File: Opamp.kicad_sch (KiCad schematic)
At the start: 51 parts, among them Q2 NPN, Q3 NPN, U1 ADA4522-2ARMZ-R7, U10 2N7002KDW_R1_00001, U11 2N7002KDW_R1_00001, U2 TCA9535RTWR, U4 2N7002KDW_R1_00001, U5 2N7002KDW_R1_00001, U6 2N7002KDW_R1_00001, U7 2N7002KDW_R1_00001, U8 2N7002KDW_R1_00001, U9 2N7002KDW_R1_00001

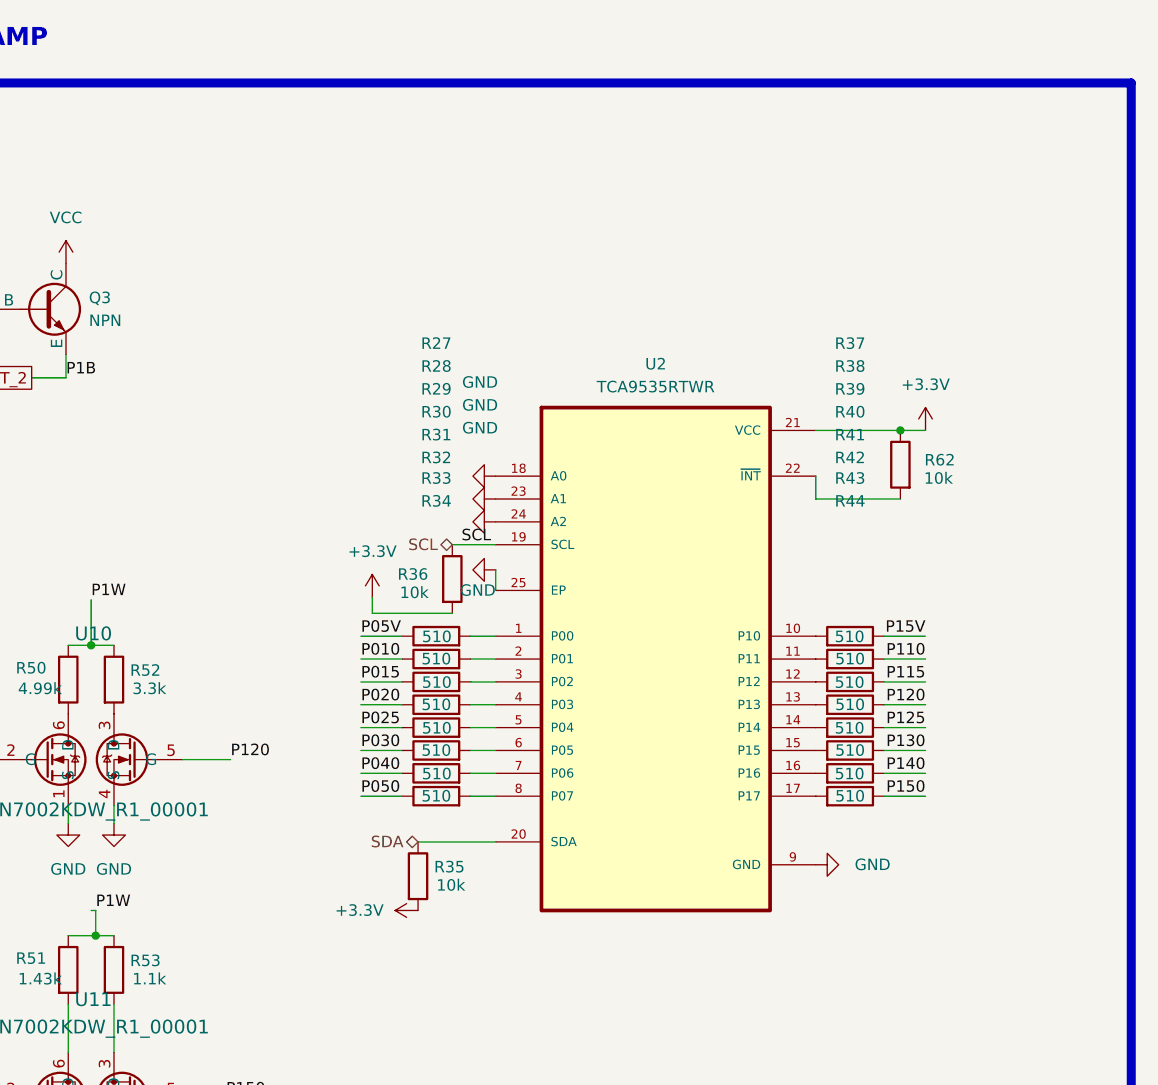
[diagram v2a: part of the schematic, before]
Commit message: version 4: changed GPIO expander, added current sense resistor to electrodes, added buzzer pins, fixed some gpio inputs that needs to be pulled high, added battery charge detection, added battery level measurement feature
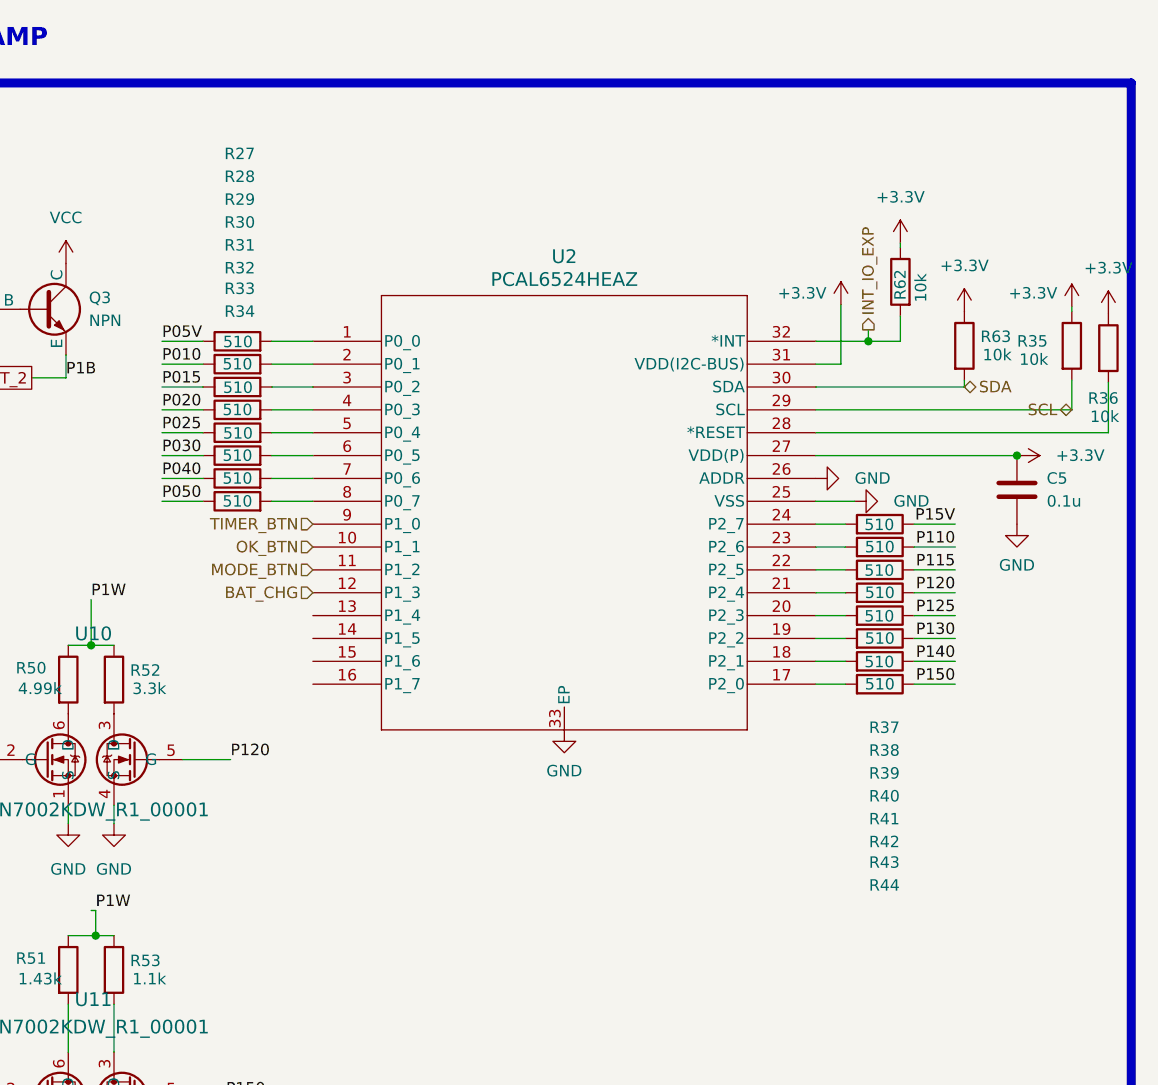
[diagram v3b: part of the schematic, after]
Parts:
- removed U2: TCA9535RTWR, Library:QFN50P400X400X80-25N, symbol 2023-09-03_14-36-57:TCA9535RTWR
- added C5: 0.1u, Capacitor_SMD:C_0402_1005Metric, symbol Device:C
- added R63: 10k, Resistor_SMD:R_0402_1005Metric, symbol Device:R
- added U2: PCAL6524HEAZ, Library:HUQFN32_PCAL6524_NXP, symbol 2023-09-03_14-36-57:PCAL6524HEAZ
- U1: Long Description (none) -> Zero-Drift Amplifier 2 Circuit Rail-to-Rail 8-MSOP
- U10, U11, U4, U5, U6, U7, U8, U9: Long Description (none) -> Mosfet Array 60V 115mA (Ta) 200mW (Ta) Surface Mount SOT-363
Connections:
- net +3.3V: now also R35.1, R36.1, C5.2, R63.1, U2.27 (VDD(P)), U2.31 (VDD(I2C-BUS)); no longer R35.2, R36.2
- net GND: now also C5.1, U2.25 (VSS), U2.26 (ADDR), U2.33 (EP)
- net SCL: now also R35.2, U2.29 (SCL); no longer R36.1
- net SDA: now also R63.2, U2.30 (SDA); no longer R35.1
- net at R41.2: now also U2.20 (P2_3)
- net at R31.2: now also U2.5 (P0_4)
- net at R30.2: now also U2.4 (P0_3)
- net at R44.2: now also U2.17 (P2_0)
- net at R37.2: now also U2.24 (P2_7)
- net INT_IO_EXP: now reaches R62.2
- net INT_IO_EXP: now also U2.32 (*INT)
- net at R27.2: now also U2.1 (P0_0)
- net at R38.2: now also U2.23 (P2_6)
- net at R39.2: now also U2.22 (P2_5)
- net at R40.2: now also U2.21 (P2_4)
- net at R42.2: now also U2.19 (P2_2)
- net at R43.2: now also U2.18 (P2_1)
- net at R28.2: now also U2.2 (P0_1)
- net at R29.2: now also U2.3 (P0_2)
- net at R32.2: now also U2.6 (P0_5)
- net at R33.2: now also U2.7 (P0_6)
- net at R34.2: now also U2.8 (P0_7)
- new net: R36.2, U2.28 (*RESET)
- new net BAT_CHG: U2.12 (P1_3)
- new net MODE_BTN: U2.11 (P1_2)
- new net OK_BTN: U2.10 (P1_1)
- new net TIMER_BTN: U2.9 (P1_0)
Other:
- moved on the sheet: R27, R28, R29, R30, R31, R32, R33, R34, R37, R38, R39, R40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

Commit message: version 5: replaced ESP32-WROVER module with ESP-Mini, removed 2.5mm plugs, changed USB connector and routed electrode signals on it, added RC snubber circuit to boost converter and output caps to reduce switching loop
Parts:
- Q2, Q3: Long Description Bipolar (BJT) Transistor NPN 60 V 2 A 100MHz 460 mW Surface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 -> Bipolar (BJT) Transistor NPN 60 V 1 A 150MHz 460 mW Surface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; Manufacturer On Semiconductor -> Diodes Incorporated; Manufacturer Part Number NSS60201LT1G -> DNBT8105-7
- R11, R45: Manufacturer Part Number RC0402FR-1016KL -> RC0402FR-0716KL
- R27, R28, R29, R30, R31, R32, R33, R34, R37, R38, R39, R40, R41, R42, R43, R44: Manufacturer Part Number RC0402FR-10510RL -> RC0402FR-07510RL
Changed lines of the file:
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@@
       (effects (font (size 1.27 1.27)) hide)
     )
-    (property "Manufacturer" "On Semiconductor" (at 130.81 47.244 0)
+    (property "Manufacturer" "Diodes Incorporated" (at 130.81 47.244 0)
       (effects (font (size 1.27 1.27)) hide)
     )
-    (property "Manufacturer Part Number" "NSS60201LT1G" (at 130.81 47.244 0)
+    (property "Manufacturer Part Number" "DNBT8105-7" (at 130.81 47.244 0)
       (effects (font (size 1.27 1.27)) hide)
     )
-    (property "Description" "TRANS NPN 60V 2A SOT23-3" (at 130.81 47.244 0)
+    (property "Description" "TRANS NPN 60V 1A SOT23-3" (at 130.81 47.244 0)
       (effects (font (size 1.27 1.27)) hide)
     )
-    (property "Long Description" "Bipolar (BJT) Transistor NPN 60 V 2 A 100MHz 460 mW Surface Mount SOT-23-3 (TO-236)" (at 130.81 47.244 0)
+    (property "Long Description" "Bipolar (BJT) Transistor NPN 60 V 1 A 150MHz 460 mW Surface Mount SOT-23-3 (TO-236)" (at 130.81 47.244 0)
       (effects (font (size 1.27 1.27)) hide)
     )
@@
       (effects (font (size 1.27 1.27)) hide)
     )
-    (property "Manufacturer Part Number" "RC0402FR-10510RL" (at 246.888 81.28 0)
+    (property "Manufacturer Part Number" "RC0402FR-07510RL" (at 246.888 81.28 0)
       (effects (font (size 1.27 1.27)) hide)
     )
@@
       (effects (font (size 1.27 1.27)) hide)
     )
-    (property "Manufacturer Part Number" "RC0402FR-10510RL" (at 175.514 60.96 0)
+    (property "Manufacturer Part Number" "RC0402FR-07510RL" (at 175.514 60.96 0)
       (effects (font (size 1.27 1.27)) hide)
     )
@@
       (effects (font (size 1.27 1.27)) hide)
     )
-    (property "Manufacturer Part Number" "RC0402FR-10510RL" (at 175.514 58.42 0)
+    (property "Manufacturer Part Number" "RC0402FR-07510RL" (at 175.514 58.42 0)
       (effects (font (size 1.27 1.27)) hide)
     )
@@
       (effects (font (size 1.27 1.27)) hide)
     )
-    (property "Manufacturer Part Number" "RC0402FR-10510RL" (at 246.888 88.9 0)
+    (property "Manufacturer Part Number" "RC0402FR-07510RL" (at 246.888 88.9 0)
       (effects (font (size 1.27 1.27)) hide)
     )
@@
       (effects (font (size 1.27 1.27)) hide)
     )
-    (property "Manufacturer Part Number" "RC0402FR-10510RL" (at 246.888 71.12 0)
+    (property "Manufacturer Part Number" "RC0402FR-07510RL" (at 246.888 71.12 0)
       (effects (font (size 1.27 1.27)) hide)
     )
@@
       (effects (font (size 1.27 1.27)) hide)
     )
-    (property "Manufacturer Part Number" "RC0402FR-10510RL" (at 175.514 66.04 0)
+    (property "Manufacturer Part Number" "RC0402FR-07510RL" (at 175.514 66.04 0)
       (effects (font (size 1.27 1.27)) hide)
     )
@@
       (effects (font (size 1.27 1.27)) hide)
     )
-    (property "Manufacturer Part Number" "RC0402FR-10510RL" (at 246.888 78.74 0)
+    (property "Manufacturer Part Number" "RC0402FR-07510RL" (at 246.888 78.74 0)
       (effects (font (size 1.27 1.27)) hide)
     )
@@
       (effects (font (size 1.27 1.27)) hide)
     )
-    (property "Manufacturer Part Number" "RC0402FR-1016KL" (at 35.814 44.45 0)
+    (property "Manufacturer Part Number" "RC0402FR-0716KL" (at 35.814 44.45 0)
       (effects (font (size 1.27 1.27)) hide)
     )
@@
       (effects (font (size 1.27 1.27)) hide)
     )
-    (property "Manufacturer Part Number" "RC0402FR-10510RL" (at 246.888 83.82 0)
+    (property "Manufacturer Part Number" "RC0402FR-07510RL" (at 246.888 83.82 0)
       (effects (font (size 1.27 1.27)) hide)
     )
@@
       (effects (font (size 1.27 1.27)) hide)
     )
-    (property "Manufacturer Part Number" "RC0402FR-10510RL" (at 175.514 68.58 0)
+    (property "Manufacturer Part Number" "RC0402FR-07510RL" (at 175.514 68.58 0)
       (effects (font (size 1.27 1.27)) hide)
     )
@@
       (effects (font (size 1.27 1.27)) hide)
     )
-    (property "Manufacturer Part Number" "RC0402FR-10510RL" (at 175.514 63.5 0)
+    (property "Manufacturer Part Number" "RC0402FR-07510RL" (at 175.514 63.5 0)
       (effects (font (size 1.27 1.27)) hide)
     )
@@
       (effects (font (size 1.27 1.27)) hide)
     )
-    (property "Manufacturer Part Number" "RC0402FR-10510RL" (at 246.888 86.36 0)
+    (property "Manufacturer Part Number" "RC0402FR-07510RL" (at 246.888 86.36 0)
       (effects (font (size 1.27 1.27)) hide)
     )
@@
       (effects (font (size 1.27 1.27)) hide)
     )
-    (property "Manufacturer Part Number" "RC0402FR-10510RL" (at 175.514 50.8 0)
+    (property "Manufacturer Part Number" "RC0402FR-07510RL" (at 175.514 50.8 0)
       (effects (font (size 1.27 1.27)) hide)
     )
@@
       (effects (font (size 1.27 1.27)) hide)
     )
-    (property "Manufacturer Part Number" "RC0402FR-10510RL" (at 175.514 55.88 0)
+    (property "Manufacturer Part Number" "RC0402FR-07510RL" (at 175.514 55.88 0)
       (effects (font (size 1.27 1.27)) hide)
     )
@@
       (effects (font (size 1.27 1.27)) hide)
     )
-    (property "Manufacturer Part Number" "RC0402FR-10510RL" (at 175.514 53.34 0)
+    (property "Manufacturer Part Number" "RC0402FR-07510RL" (at 175.514 53.34 0)
       (effects (font (size 1.27 1.27)) hide)
     )
@@
       (effects (font (size 1.27 1.27)) hide)
     )
-    (property "Manufacturer Part Number" "RC0402FR-10510RL" (at 246.888 76.2 0)
+    (property "Manufacturer Part Number" "RC0402FR-07510RL" (at 246.888 76.2 0)
       (effects (font (size 1.27 1.27)) hide)
     )
@@
       (effects (font (size 1.27 1.27)) hide)
     )
-    (property "Manufacturer" "On Semiconductor" (at 153.924 47.244 0)
+    (property "Manufacturer" "Diodes Incorporated" (at 153.924 47.244 0)
       (effects (font (size 1.27 1.27)) hide)
     )
-    (property "Manufacturer Part Number" "NSS60201LT1G" (at 153.924 47.244 0)
+    (property "Manufacturer Part Number" "DNBT8105-7" (at 153.924 47.244 0)
       (effects (font (size 1.27 1.27)) hide)
     )
-    (property "Description" "TRANS NPN 60V 2A SOT23-3" (at 153.924 47.244 0)
+    (property "Description" "TRANS NPN 60V 1A SOT23-3" (at 153.924 47.244 0)
       (effects (font (size 1.27 1.27)) hide)
     )
-    (property "Long Description" "Bipolar (BJT) Transistor NPN 60 V 2 A 100MHz 460 mW Surface Mount SOT-23-3 (TO-236)" (at 153.924 47.244 0)
+    (property "Long Description" "Bipolar (BJT) Transistor NPN 60 V 1 A 150MHz 460 mW Surface Mount SOT-23-3 (TO-236)" (at 153.924 47.244 0)
       (effects (font (size 1.27 1.27)) hide)
     )
@@
       (effects (font (size 1.27 1.27)) hide)
     )
-    (property "Manufacturer Part Number" "RC0402FR-1016KL" (at 109.22 46.736 0)
+    (property "Manufacturer Part Number" "RC0402FR-0716KL" (at 109.22 46.736 0)
       (effects (font (size 1.27 1.27)) hide)
     )
@@
       (effects (font (size 1.27 1.27)) hide)
     )
-    (property "Manufacturer Part Number" "RC0402FR-10510RL" (at 246.888 73.66 0)
+    (property "Manufacturer Part Number" "RC0402FR-07510RL" (at 246.888 73.66 0)
       (effects (font (size 1.27 1.27)) hide)
     )

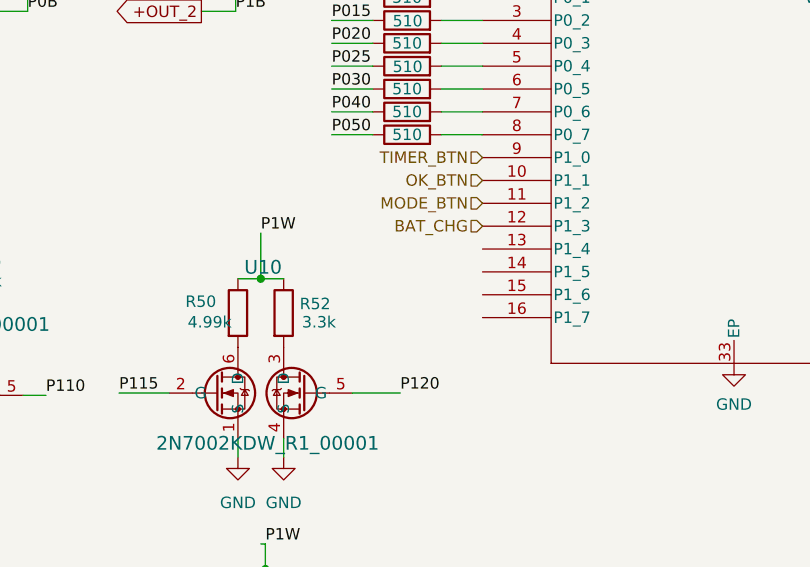
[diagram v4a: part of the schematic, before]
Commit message: Fixed electrode detection mechanism, modified position of USB Type-C port
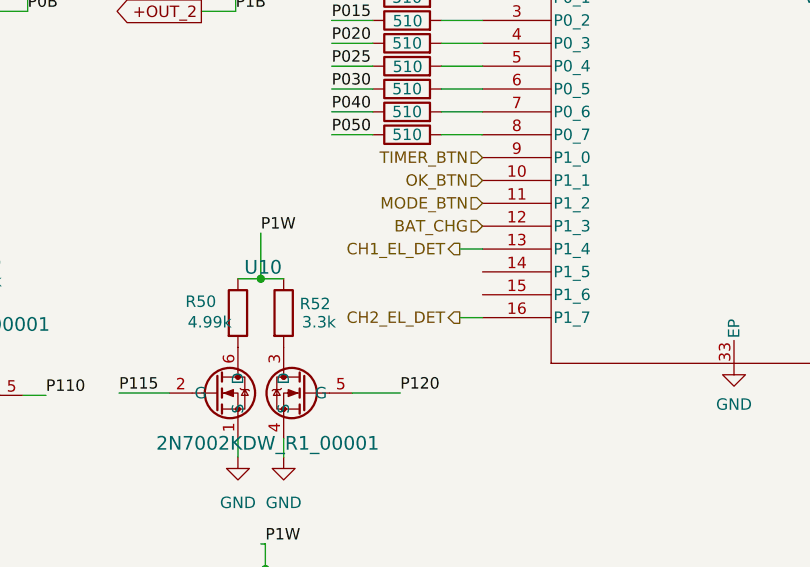
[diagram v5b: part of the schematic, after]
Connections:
- net CH1_EL_DET: now reaches U2.13 (P1_4)
- net CH2_EL_DET: now reaches U2.16 (P1_7)
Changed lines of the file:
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@@
+    (stroke (width 0) (type default))
+  )
+  (wire (pts (xy 181.356 81.28) (xy 183.896 81.28))
     (stroke (width 0) (type default))
   )
@@
   )
   (wire (pts (xy 255.27 73.66) (xy 250.698 73.66))
+    (stroke (width 0) (type default))
+  )
+  (wire (pts (xy 181.356 88.9) (xy 183.896 88.9))
     (stroke (width 0) (type default))
   )
@@
     (effects (font (size 1.27 1.27)) (justify left))
   )
+  (hierarchical_label "CH2_EL_DET" (shape output) (at 181.356 88.9 180) (fields_autoplaced)
+    (effects (font (size 1.27 1.27)) (justify right))
+  )
   (hierarchical_label "TIMER_BTN" (shape input) (at 183.896 71.12 180) (fields_autoplaced)
     (effects (font (size 1.27 1.27)) (justify right))
   )
+  (hierarchical_label "CH1_EL_DET" (shape output) (at 181.356 81.28 180) (fields_autoplaced)
+    (effects (font (size 1.27 1.27)) (justify right))
+  )
